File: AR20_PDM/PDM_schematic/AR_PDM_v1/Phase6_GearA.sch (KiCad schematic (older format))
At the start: 14 parts, among them Q17 N_FET, Q6 BTS50025-1TAD, U8 INA233

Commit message: Alpha version DONE! - Gerber files generated
- Tweeked
- checked and re cheked
- added all missing components
- Created a really nice silkscreen
- Ready To Test
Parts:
- renumbered C_in3 to C22, C_out3 to C23, C_vs3 to C24, Cs3 to C25, C_bypass6 to C26, Q17 to Q4, Q6 to Q5, R58 to R19, R9 to R20, R_in3 to R21, R_sense3 to R22, R_s3 to R23, R_Shunt7 to R24, U8 to U5

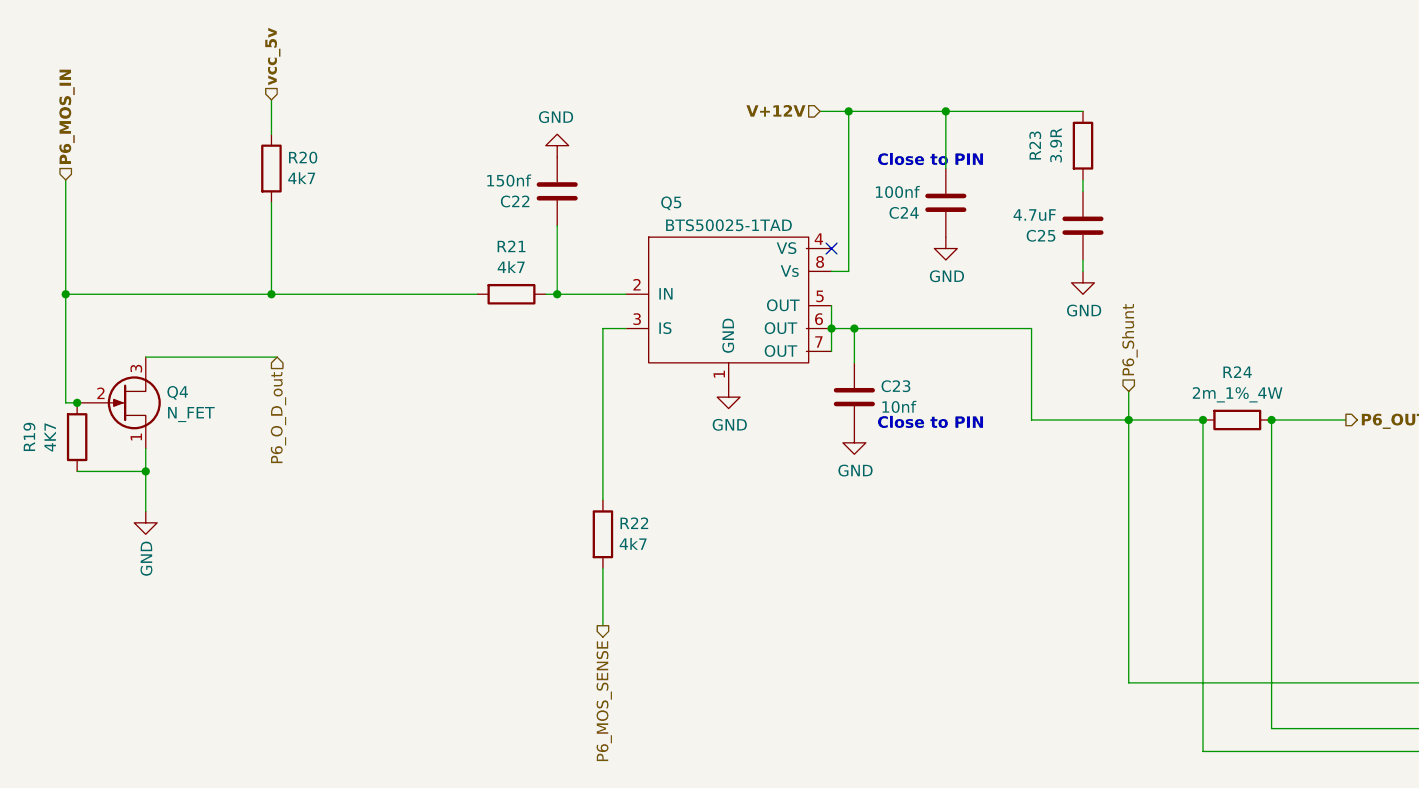
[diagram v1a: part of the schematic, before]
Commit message: Fixed wrong resistors, mos sense. Gerber files updated
- removed all R_is_protection resistors on each mosfet line
- added one R_is_protection resistors to mos_sense_all
ps, mux N-fets, does not need overvoltage protection. 60 volt tolerant.
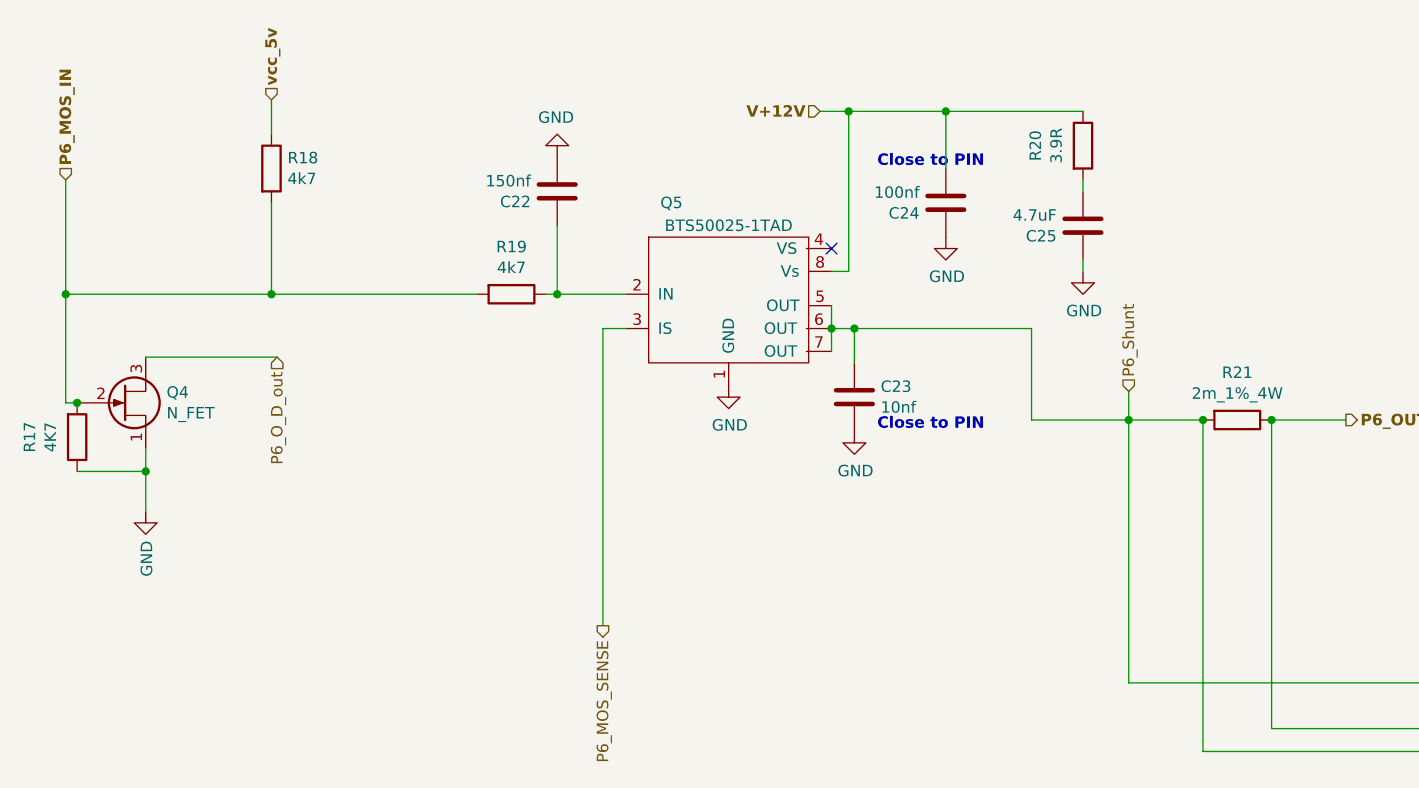
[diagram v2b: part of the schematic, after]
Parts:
- removed R22: 4k7, Resistor_SMD:R_0603_1608Metric, symbol AR20_PDM_v1-rescue:R-Device
- renumbered R19 to R17, R20 to R18, R21 to R19, R23 to R20, R24 to R21
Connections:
- net P6_MOS_SENSE: now also Q5.3 (IS)
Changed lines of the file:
@@
 AR Path="/5E0FC3A2/5E21B806" Ref="R?"  Part="1"
 AR Path="/5E0FCFDC/5E21B806" Ref="R?"  Part="1"
-AR Path="/5E0FDCCC/5E21B806" Ref="R21"  Part="1"
+AR Path="/5E0FDCCC/5E21B806" Ref="R19"  Part="1"
 AR Path="/5E10174B/5E21B806" Ref="R?"  Part="1"
-F 0 "R21" V 3093 2400 50  0000 C CNN
+F 0 "R19" V 3093 2400 50  0000 C CNN
 F 1 "4k7" V 3184 2400 50  0000 C CNN
 F 2 "Resistor_SMD:R_0603_1608Metric" V 3230 2400 50  0001 C CNN
@@
 AR Path="/5E0FC3A2/5DAAC1E9" Ref="R?"  Part="1"
 AR Path="/5E0FCFDC/5DAAC1E9" Ref="R?"  Part="1"
-AR Path="/5E0FDCCC/5DAAC1E9" Ref="R20"  Part="1"
+AR Path="/5E0FDCCC/5DAAC1E9" Ref="R18"  Part="1"
 AR Path="/5E10174B/5DAAC1E9" Ref="R?"  Part="1"
-F 0 "R20" H 2320 1896 50  0000 L CNN
+F 0 "R18" H 2320 1896 50  0000 L CNN
 F 1 "4k7" H 2320 1805 50  0000 L CNN
 F 2 "Resistor_SMD:R_0603_1608Metric" V 2180 1850 50  0001 C CNN
@@
 	3700 2550 3800 2550
 Wire Wire Line
-	3700 3850 3700 3600
-Wire Wire Line
 	8750 2850 8750 3350
 Wire Wire Line
@@
 AR Path="/5E0FC3A2/5E21B86D" Ref="R?"  Part="1"
 AR Path="/5E0FCFDC/5E21B86D" Ref="R?"  Part="1"
-AR Path="/5E0FDCCC/5E21B86D" Ref="R23"  Part="1"
+AR Path="/5E0FDCCC/5E21B86D" Ref="R20"  Part="1"
 AR Path="/5E10174B/5E21B86D" Ref="R?"  Part="1"
-F 0 "R23" V 5593 1750 50  0000 C CNN
+F 0 "R20" V 5593 1750 50  0000 C CNN
 F 1 "3.9R" V 5684 1750 50  0000 C CNN
 F 2 "Resistor_SMD:R_0603_1608Metric" V 5730 1750 50  0001 C CNN
@@
 Wire Wire Line
 	6000 4100 8750 4100
-$Comp
-L AR20_PDM_v1-rescue:R-Device R?
-U 1 1 5E21B873
-P 3700 3450
-AR Path="/5DA89415/5E21B873" Ref="R?"  Part="1"
-AR Path="/5DEB10A1/5E21B873" Ref="R?"  Part="1"
-AR Path="/5DEB20EA/5E21B873" Ref="R?"  Part="1"
-AR Path="/5E0E4725/5E21B873" Ref="R?"  Part="1"
-AR Path="/5E0E4A93/5E21B873" Ref="R?"  Part="1"
-AR Path="/5E0E4EB5/5E21B873" Ref="R?"  Part="1"
-AR Path="/5E0E5304/5E21B873" Ref="R?"  Part="1"
-AR Path="/5E0E594B/5E21B873" Ref="R?"  Part="1"
-AR Path="/5E0E607C/5E21B873" Ref="R?"  Part="1"
-AR Path="/5E0FB5C8/5E21B873" Ref="R?"  Part="1"
-AR Path="/5E0FBBBD/5E21B873" Ref="R?"  Part="1"
-AR Path="/5E0FC3A2/5E21B873" Ref="R?"  Part="1"
-AR Path="/5E0FCFDC/5E21B873" Ref="R?"  Part="1"
-AR Path="/5E0FDCCC/5E21B873" Ref="R22"  Part="1"
-AR Path="/5E10174B/5E21B873" Ref="R?"  Part="1"
-F 0 "R22" H 3770 3496 50  0000 L CNN
-F 1 "4k7" H 3770 3405 50  0000 L CNN
-F 2 "Resistor_SMD:R_0603_1608Metric" V 3630 3450 50  0001 C CNN
-F 3 "~" H 3700 3450 50  0001 C CNN
-	1    3700 3450
-	1    0    0    -1
-$EndComp
 Wire Wire Line
 	6325 4400 8750 4400
@@
 AR Path="/5E0FC3A2/5E1DA63E" Ref="R?"  Part="1"
 AR Path="/5E0FCFDC/5E1DA63E" Ref="R?"  Part="1"
-AR Path="/5E0FDCCC/5E1DA63E" Ref="R24"  Part="1"
+AR Path="/5E0FDCCC/5E1DA63E" Ref="R21"  Part="1"
 AR Path="/5E10174B/5E1DA63E" Ref="R?"  Part="1"
-F 0 "R24" V 6268 2950 50  0000 C CNN
+F 0 "R21" V 6268 2950 50  0000 C CNN
 F 1 "2m_1%_4W" V 6359 2950 50  0000 C CNN
 F 2 "Resistor_SMD:R_2512_6332Metric" V 6405 2950 50  0001 C CNN
@@
 AR Path="/5DA8920B/5E25DA34" Ref="R?"  Part="1"
 AR Path="/5E2546F2/5E25DA34" Ref="R?"  Part="1"
-AR Path="/5E0FDCCC/5E25DA34" Ref="R19"  Part="1"
-F 0 "R19" V 1193 3025 50  0000 C CNN
+AR Path="/5E0FDCCC/5E25DA34" Ref="R17"  Part="1"
+F 0 "R17" V 1193 3025 50  0000 C CNN
 F 1 "4K7" V 1284 3025 50  0000 C CNN
 F 2 "Resistor_SMD:R_0603_1608Metric" V 1330 3025 50  0001 C CNN
@@
 Connection ~ 6000 2950
 Wire Wire Line
-	3700 2550 3700 3300
-Wire Wire Line
 	4650 1600 4775 1600
 Wire Wire Line
@@
 Wire Wire Line
 	4775 1600 5200 1600
+Wire Wire Line
+	3700 2550 3700 3850
 $EndSCHEMATC

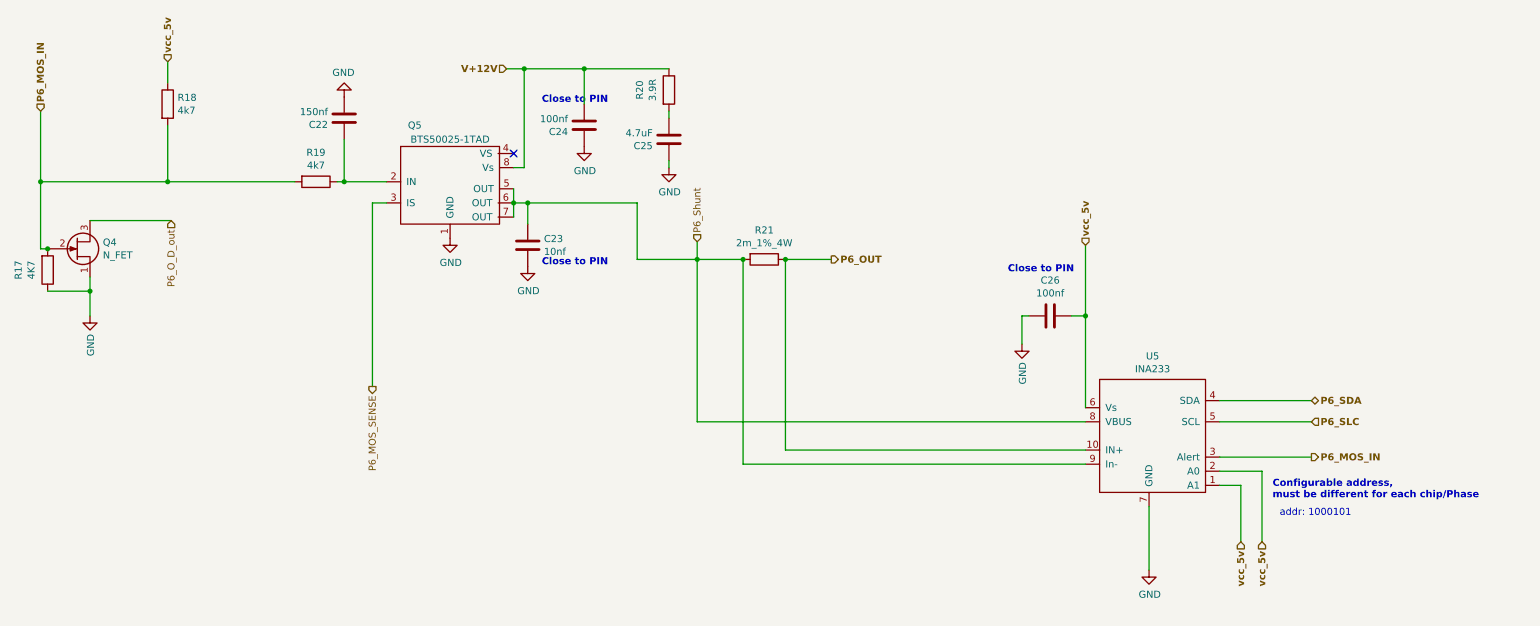
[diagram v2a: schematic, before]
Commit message: Major redesign. schematics completed, PCB work in progress
-TODO : A proper changelog file. Where all changes will apear 
- Redesigned schematics to accommodate errors in the improvement list
- More detail in ALPHA improvement list
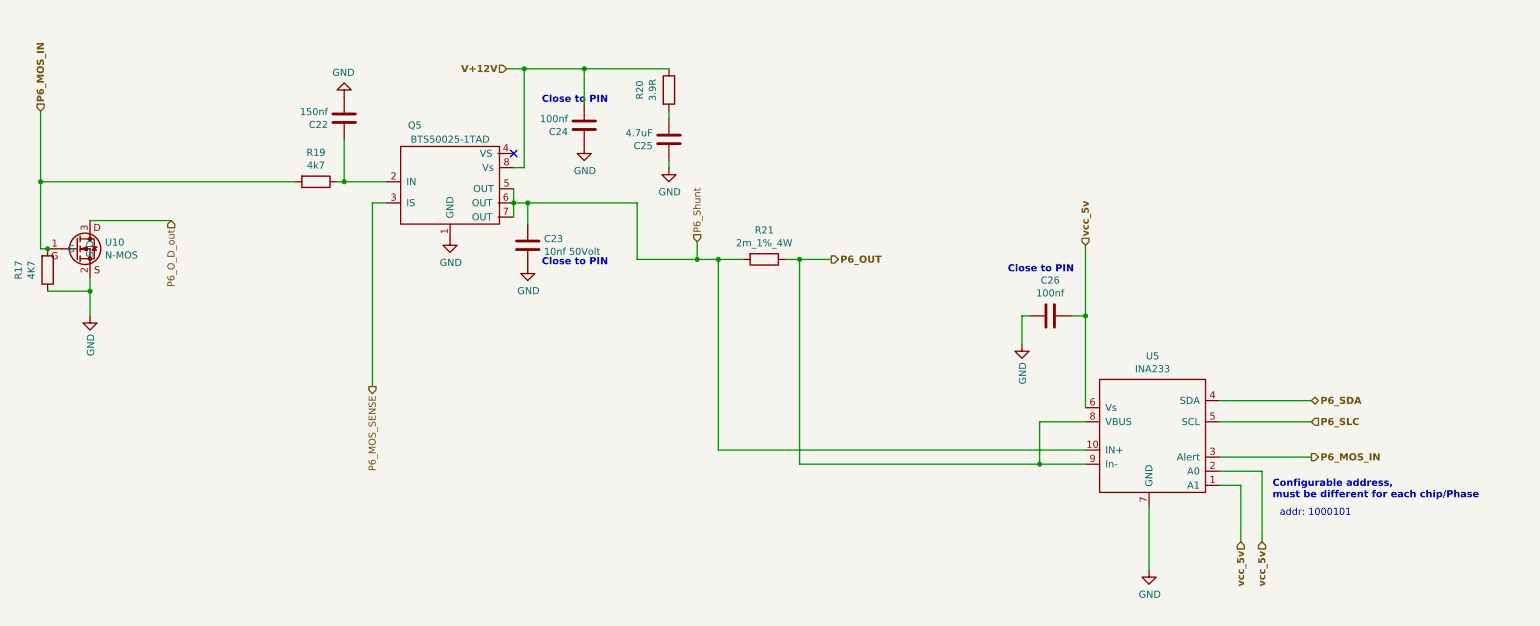
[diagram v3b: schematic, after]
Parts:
- removed Q4: N_FET, Package_TO_SOT_SMD:SOT-23, symbol Device:Q_NJFET_DGS
- removed R18: 4k7, Resistor_SMD:R_0603_1608Metric, symbol AR20_PDM_v1-rescue:R-Device
- added U10: N-MOS, AR_PDM_v1:N-MOS-DMN6140L-13, symbol AR20_PDM_v1-rescue:N-MOS-DMN6140L-13
- C23: value 10nf -> 10nf 50Volt
- R20: footprint Resistor_SMD:R_0603_1608Metric -> Resistor_SMD:R_2512_6332Metric
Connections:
- net GND: now also U10.2 (S)
- net P6_MOS_IN: now also U10.1 (G)
- net P6_OUT: now also U5.8 (VBUS), U5.9 (In-); no longer U5.10 (IN+)
- net P6_O_D_out: now also U10.3 (D)
- net P6_Shunt: now also U5.10 (IN+); no longer U5.8 (VBUS), U5.9 (In-)
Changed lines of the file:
@@
 $Descr A4 11693 8268
 encoding utf-8
-Sheet 5 13
+Sheet 5 14
 Title ""
 Date ""
@@
 AR Path="/5E10174B/5DAAC1D1" Ref="C?"  Part="1"
 F 0 "C23" H 4915 2896 50  0000 L CNN
-F 1 "10nf" H 4915 2805 50  0000 L CNN
+F 1 "10nf 50Volt" H 4915 2805 50  0000 L CNN
 F 2 "Capacitor_SMD:C_0603_1608Metric" H 4838 2700 50  0001 C CNN
 F 3 "~" H 4800 2850 50  0001 C CNN
@@
 $EndComp
 $Comp
-L AR20_PDM_v1-rescue:R-Device R?
-U 1 1 5DAAC1E9
-P 2250 1850
-AR Path="/5DA89415/5DAAC1E9" Ref="R?"  Part="1"
-AR Path="/5DEB10A1/5DAAC1E9" Ref="R?"  Part="1"
-AR Path="/5DEB20EA/5DAAC1E9" Ref="R?"  Part="1"
-AR Path="/5E0E4725/5DAAC1E9" Ref="R?"  Part="1"
-AR Path="/5E0E4A93/5DAAC1E9" Ref="R?"  Part="1"
-AR Path="/5E0E4EB5/5DAAC1E9" Ref="R?"  Part="1"
-AR Path="/5E0E5304/5DAAC1E9" Ref="R?"  Part="1"
-AR Path="/5E0E594B/5DAAC1E9" Ref="R?"  Part="1"
-AR Path="/5E0E607C/5DAAC1E9" Ref="R?"  Part="1"
-AR Path="/5E0FB5C8/5DAAC1E9" Ref="R?"  Part="1"
-AR Path="/5E0FBBBD/5DAAC1E9" Ref="R?"  Part="1"
-AR Path="/5E0FC3A2/5DAAC1E9" Ref="R?"  Part="1"
-AR Path="/5E0FCFDC/5DAAC1E9" Ref="R?"  Part="1"
-AR Path="/5E0FDCCC/5DAAC1E9" Ref="R18"  Part="1"
-AR Path="/5E10174B/5DAAC1E9" Ref="R?"  Part="1"
-F 0 "R18" H 2320 1896 50  0000 L CNN
-F 1 "4k7" H 2320 1805 50  0000 L CNN
-F 2 "Resistor_SMD:R_0603_1608Metric" V 2180 1850 50  0001 C CNN
-F 3 "~" H 2250 1850 50  0001 C CNN
-	1    2250 1850
-	1    0    0    -1
-$EndComp
-$Comp
 L AR20_PDM_v1-rescue:C-Device C?
 U 1 1 5E21B824
@@
 Text Notes 8200 3050 0    50   ~ 10
 Close to PIN
-Text HLabel 2250 1550 1    50   Input ~ 10
-vcc_5v
 Wire Wire Line
 	9700 4100 10350 4100
-Wire Wire Line
-	2250 1550 2250 1700
 $Comp
 L AR20_PDM_v1-rescue:C-Device C?
@@
 F 0 "R20" V 5593 1750 50  0000 C CNN
 F 1 "3.9R" V 5684 1750 50  0000 C CNN
-F 2 "Resistor_SMD:R_0603_1608Metric" V 5730 1750 50  0001 C CNN
+F 2 "Resistor_SMD:R_2512_6332Metric" V 5730 1750 50  0001 C CNN
 F 3 "~" H 5800 1750 50  0001 C CNN
 	1    5800 1750
@@
 Wire Wire Line
 	9700 4350 10350 4350
-Connection ~ 2250 2400
-Wire Wire Line
-	2250 2000 2250 2400
 Wire Wire Line
 	1350 1900 1350 2400
@@
 	5575 2550 5575 2950
 Connection ~ 4800 2550
-Wire Wire Line
-	6000 4100 8750 4100
-Wire Wire Line
-	6325 4400 8750 4400
-Wire Wire Line
-	6625 4300 8750 4300
 Text HLabel 3700 3850 3    50   Output ~ 0
 P6_MOS_SENSE
-Wire Wire Line
-	6000 4100 6000 2950
 Wire Wire Line
 	5575 2950 6000 2950
@@
 V+12V
 Wire Wire Line
-	2250 2400 3150 2400
-Wire Wire Line
-	6625 2950 6625 4300
-Wire Wire Line
-	6325 2950 6325 4400
-Wire Wire Line
-	6000 2950 6325 2950
+	6000 2950 6150 2950
 $Comp
 L AR20_PDM_v1-rescue:R-Device R?
@@
 $EndComp
 Wire Wire Line
-	6625 2950 6950 2950
-Connection ~ 6325 2950
-Connection ~ 6625 2950
+	6625 2950 6725 2950
 Text Notes 10125 4775 0    50   ~ 0
 addr: 1000101
@@
 Wire Wire Line
 	1400 3175 1700 3175
-Connection ~ 1400 2875
 Wire Wire Line
 	1400 2875 1350 2875
@@
 F 3 "~" H 1400 3025 50  0001 C CNN
 	1    1400 3025
-	1    0    0    1
-$EndComp
-$Comp
-L Device:Q_NJFET_DGS Q?
-U 1 1 5E25DA2E
-P 1600 2875
-AR Path="/5DA8920B/5E25DA2E" Ref="Q?"  Part="1"
-AR Path="/5E2546F2/5E25DA2E" Ref="Q?"  Part="1"
-AR Path="/5E0FDCCC/5E25DA2E" Ref="Q4"  Part="1"
-F 0 "Q4" H 1791 2829 50  0000 L CNN
-F 1 "N_FET" H 1791 2920 50  0000 L CNN
-F 2 "Package_TO_SOT_SMD:SOT-23" H 1800 2975 50  0001 C CNN
-F 3 "~" H 1600 2875 50  0001 C CNN
-	1    1600 2875
 	1    0    0    1
 $EndComp
@@
 $EndComp
 Wire Wire Line
-	1350 2400 2250 2400
-Wire Wire Line
 	1350 2400 1350 2875
 Connection ~ 1350 2400
@@
 Wire Wire Line
 	3700 2550 3700 3850
+Wire Wire Line
+	1350 2400 3150 2400
+Wire Wire Line
+	8750 4300 6150 4300
+Wire Wire Line
+	6150 4300 6150 2950
+Wire Wire Line
+	8750 4400 8425 4400
+Wire Wire Line
+	6725 4400 6725 2950
+Wire Wire Line
+	8750 4100 8425 4100
+Wire Wire Line
+	8425 4100 8425 4400
+Connection ~ 8425 4400
+Wire Wire Line
+	8425 4400 6725 4400
+Connection ~ 6150 2950
+Wire Wire Line
+	6150 2950 6325 2950
+Connection ~ 6725 2950
+Wire Wire Line
+	6725 2950 6950 2950
+$Comp
+L AR20_PDM_v1-rescue:N-MOS-DMN6140L-13 U10
+U 1 1 5E66F806
+P 1600 2675
+F 0 "U10" H 1806 2521 50  0000 L CNN
+F 1 "N-MOS" H 1806 2430 50  0000 L CNN
+F 2 "AR_PDM_v1:N-MOS-DMN6140L-13" H 1700 3125 50  0001 C CNN
+F 3 "" H 1700 3125 50  0001 C CNN
+	1    1600 2675
+	1    0    0    -1
+$EndComp
+Connection ~ 1400 2875
 $EndSCHEMATC
